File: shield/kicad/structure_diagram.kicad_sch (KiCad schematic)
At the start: 15 parts, among them J1 FCI-10118193-0001LF, J10 Amphenol SFV12R-2STE1HLF, J11 Harwin M20-8771042, J12 Harwin M20-8770842, J13 Harwin M20-8770642, J2 JST S2B-PH-SM4-TB(LF)(SN), J3 BAT_P, J4 BAT_TS, J5 BAT_M, J6 JST S3B-PH-SM4-TB(LF)(SN)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

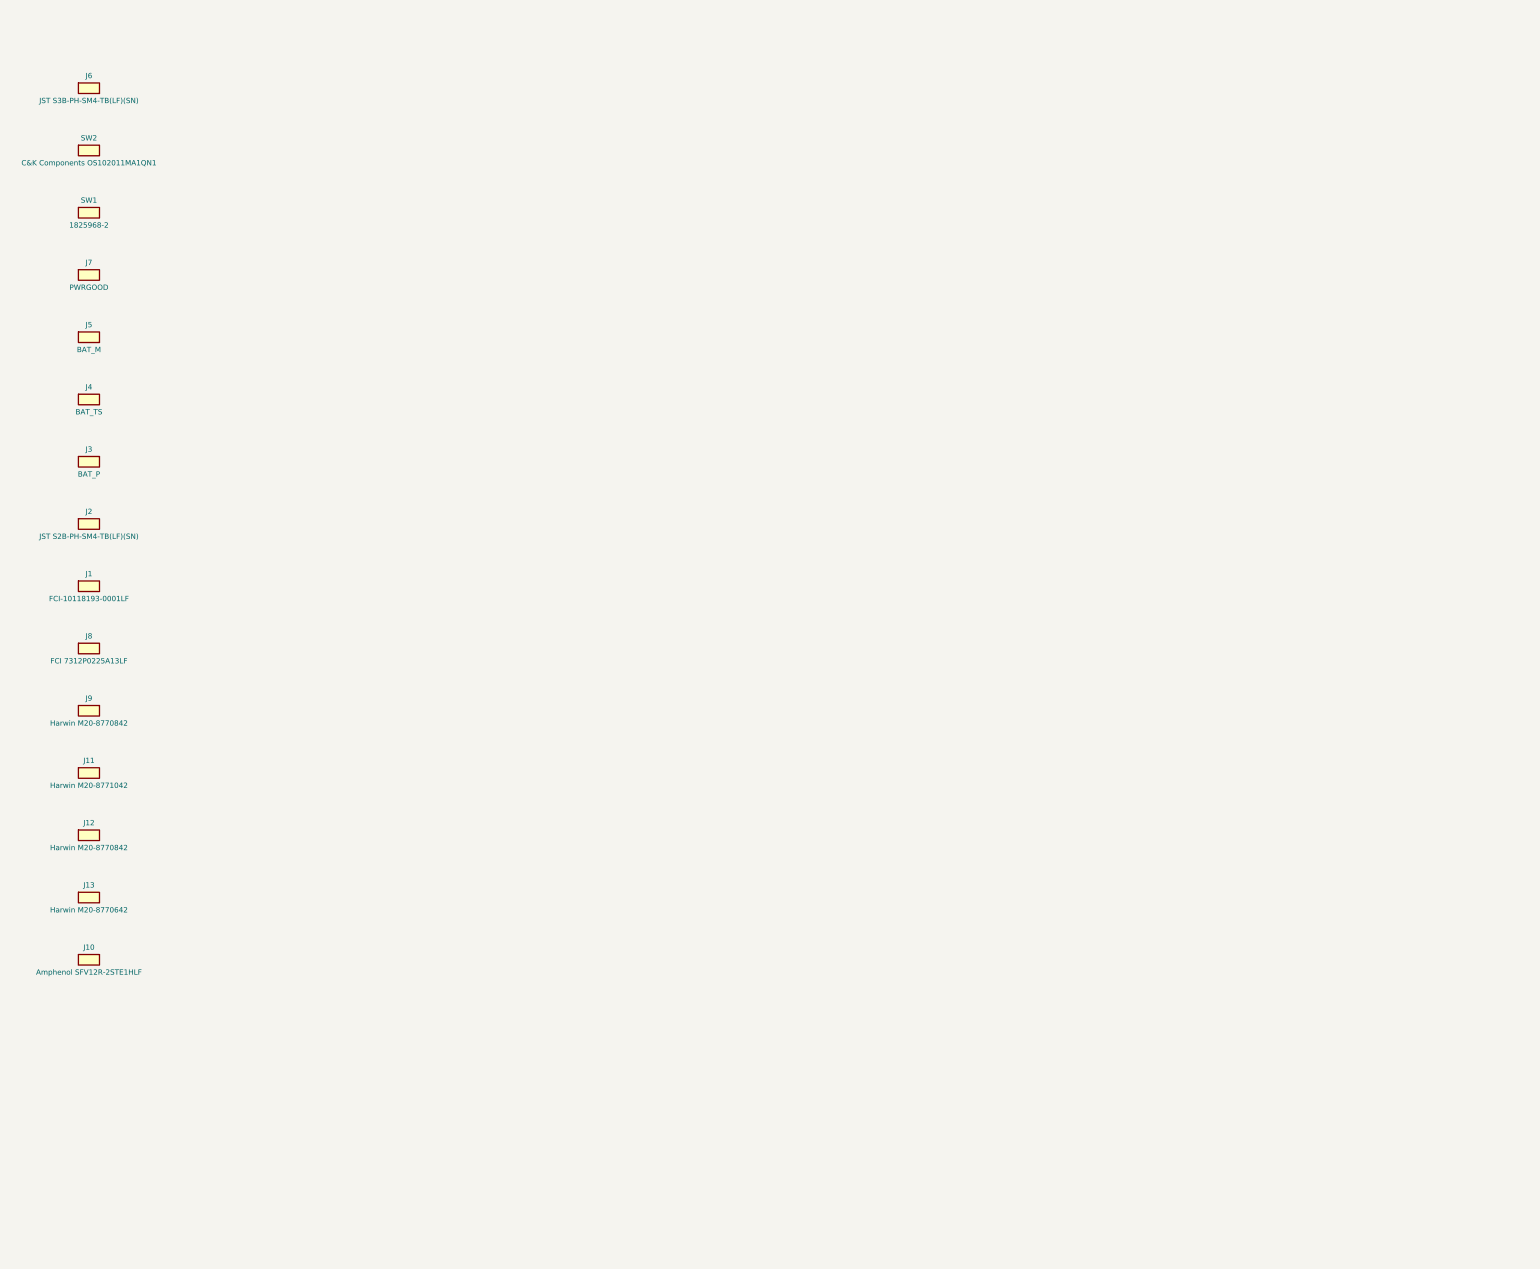
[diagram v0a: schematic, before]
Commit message: Complete schematic wiring, footprint assignments, and validation renders
- Generated proper KiCad symbols with pin definitions for all 139 components
- Created 2 hierarchical sub-sheets: Power Supply and Peripherals & Connectors
- Added schematic wiring with net labels (VBUS, VBAT, V3V3, GND, I2C, SPI, etc.)
- Assigned KiCad standard library footprints to all components
- Rendered schematic and PCB SVGs using kicad-cli-nightly
- Ran ERC and DRC validation
- Updated README with rendered images and footprint assignment table

Agent-Logs-Url: https://github.com/3rdIteration/specter-diy/sessions/67aa0d59-b533-4f87-a3fd-0109cc63ae2b

Co-authored-by: 3rdIteration <2230318+3rdIteration@users.noreply.github.com>
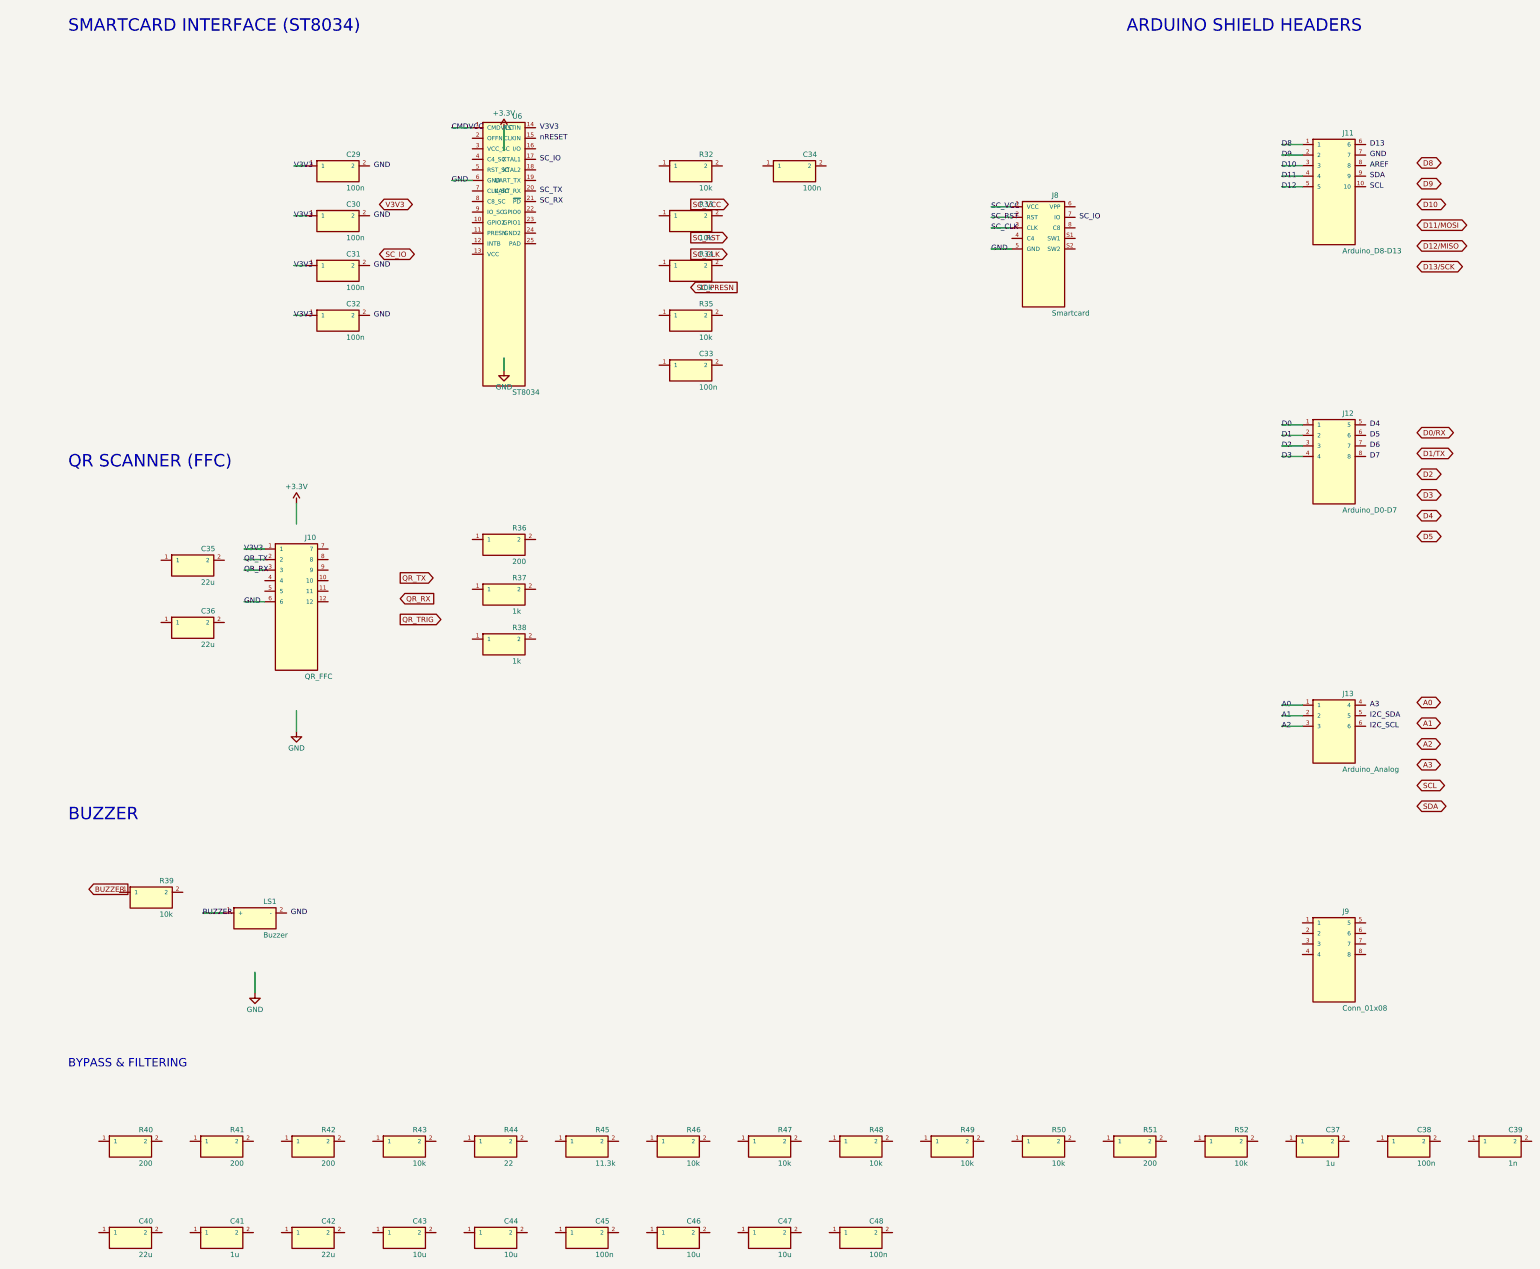
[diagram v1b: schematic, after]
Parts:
- removed J1: FCI-10118193-0001LF, MICRO-USB5+6P-SMD-0.65-B, symbol specter_shield:J1
- removed J10: Amphenol SFV12R-2STE1HLF, PCB-k5pgcgjronex5cu153ln-1, symbol specter_shield:J10
- removed J11: Harwin M20-8771042, PCB-oi3786kvfyfvus515mhx-1, symbol specter_shield:J11
- removed J12: Harwin M20-8770842, PCB-a1fsc6jjl71gcgtqmpw9-1, symbol specter_shield:J12
- removed J13: Harwin M20-8770642, PCB-tcxrerk3sfa09abtw5ob-1, symbol specter_shield:J13
- removed J2: JST S2B-PH-SM4-TB(LF)(SN), JSTPH2, symbol specter_shield:J2
- removed J3: BAT_P, PCB-zaz9lv92tniud42eyscu-1, symbol specter_shield:J3
- removed J4: BAT_TS, PCB-zaz9lv92tniud42eyscu-1, symbol specter_shield:J4
- removed J5: BAT_M, PCB-zaz9lv92tniud42eyscu-1, symbol specter_shield:J5
- removed J6: JST S3B-PH-SM4-TB(LF)(SN), PCB-icmh3e5dg0zwnj7dnv4l-1, symbol specter_shield:J6
- removed J7: PWRGOOD, PCB-16u5lfhv285szk9mzlb4-1, symbol specter_shield:J7
- removed J8: FCI 7312P0225A13LF, PCBComponent_1_-_duplicate, symbol specter_shield:J8
- removed J9: Harwin M20-8770842, PCB-a1fsc6jjl71gcgtqmpw9-1, symbol specter_shield:J9
- removed SW1: 1825968-2, PCB-y9eaa5ubtxtmw5joheuc-1, symbol specter_shield:SW1
- removed SW2: C&K Components OS102011MA1QN1, PCB-jzft20c5ocof3hhi9mdb-1, symbol specter_shield:SW2
- added C29: 100n, Capacitor_SMD:C_0402_1005Metric, symbol C29
- added C30: 100n, Capacitor_SMD:C_0402_1005Metric, symbol C30
- added C31: 100n, Capacitor_SMD:C_0402_1005Metric, symbol C31
- added C32: 100n, Capacitor_SMD:C_0402_1005Metric, symbol C32
- added C33: 100n, Capacitor_SMD:C_0402_1005Metric, symbol C33
- added C34: 100n, Capacitor_SMD:C_0402_1005Metric, symbol C34
- added C35: 22u, Capacitor_SMD:C_0805_2012Metric, symbol C35
- added C36: 22u, Capacitor_SMD:C_0805_2012Metric, symbol C36
- added C37: 1u, Capacitor_SMD:C_0402_1005Metric, symbol C37
- added C38: 100n, Capacitor_SMD:C_0402_1005Metric, symbol C38
- added C39: 1n, Capacitor_SMD:C_0402_1005Metric, symbol C39
- added C40: 22u, Capacitor_SMD:C_0805_2012Metric, symbol C40
- added C41: 1u, Capacitor_SMD:C_0402_1005Metric, symbol C41
- added C42: 22u, Capacitor_SMD:C_0805_2012Metric, symbol C42
- added C43: 10u, Capacitor_SMD:C_0805_2012Metric, symbol C43
- added C44: 10u, Capacitor_SMD:C_0805_2012Metric, symbol C44
- added C45: 100n, Capacitor_SMD:C_0402_1005Metric, symbol C45
- added C46: 10u, Capacitor_SMD:C_0805_2012Metric, symbol C46
- added C47: 10u, Capacitor_SMD:C_0805_2012Metric, symbol C47
- added C48: 100n, Capacitor_SMD:C_0402_1005Metric, symbol C48
- added J10: QR_FFC, Connector_FFC-FPC:Hirose_FH12-12S-0.5SH_1x12-1MP_P0.50mm_Horizontal, symbol J10
- added J11: Arduino_D8-D13, Connector_PinHeader_2.54mm:PinHeader_1x10_P2.54mm_Vertical, symbol J11
- added J12: Arduino_D0-D7, Connector_PinHeader_2.54mm:PinHeader_1x08_P2.54mm_Vertical, symbol J12
- added J13: Arduino_Analog, Connector_PinHeader_2.54mm:PinHeader_1x06_P2.54mm_Vertical, symbol J13
- added J8: Smartcard, Connector_Card:Smartcard_C-707-10M008-S, symbol J8
- added J9: Conn_01x08, Connector_PinHeader_2.54mm:PinHeader_1x08_P2.54mm_Vertical, symbol J9
- added LS1: Buzzer, Buzzer_Beeper:Buzzer_TDK_PS1240P02BT_D12.2mm_H6.5mm, symbol LS1
- added R32: 10k, Resistor_SMD:R_0402_1005Metric, symbol R32
- added R33: 10k, Resistor_SMD:R_0402_1005Metric, symbol R33
- added R34: 10k, Resistor_SMD:R_0402_1005Metric, symbol R34
- added R35: 10k, Resistor_SMD:R_0402_1005Metric, symbol R35
- added R36: 200, Resistor_SMD:R_0402_1005Metric, symbol R36
- added R37: 1k, Resistor_SMD:R_0402_1005Metric, symbol R37
- added R38: 1k, Resistor_SMD:R_0402_1005Metric, symbol R38
- added R39: 10k, Resistor_SMD:R_0402_1005Metric, symbol R39
- added R40: 200, Resistor_SMD:R_0402_1005Metric, symbol R40
- added R41: 200, Resistor_SMD:R_0402_1005Metric, symbol R41
- added R42: 200, Resistor_SMD:R_0402_1005Metric, symbol R42
- added R43: 10k, Resistor_SMD:R_0402_1005Metric, symbol R43
- added R44: 22, Resistor_SMD:R_0402_1005Metric, symbol R44
- added R45: 11.3k, Resistor_SMD:R_0402_1005Metric, symbol R45
- added R46: 10k, Resistor_SMD:R_0402_1005Metric, symbol R46
- added R47: 10k, Resistor_SMD:R_0402_1005Metric, symbol R47
- added R48: 10k, Resistor_SMD:R_0402_1005Metric, symbol R48
- added R49: 10k, Resistor_SMD:R_0402_1005Metric, symbol R49
- added R50: 10k, Resistor_SMD:R_0402_1005Metric, symbol R50
- added R51: 200, Resistor_SMD:R_0402_1005Metric, symbol R51
- added R52: 10k, Resistor_SMD:R_0402_1005Metric, symbol R52
- added U6: ST8034, Package_DFN_QFN:QFN-24-1EP_4x4mm_P0.5mm_EP2.45x2.45mm, symbol U6
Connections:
- new net A0: J13.1
- new net A1: J13.2
- new net A2: J13.3
- new net BUZZER: LS1.1 (+)
- new net CMDVCC: U6.1 (CMDVCC)
- new net D0: J12.1
- new net D1: J12.2
- new net D10: J11.3
- new net D11: J11.4
- new net D12: J11.5
- new net D2: J12.3
- new net D3: J12.4
- new net D8: J11.1
- new net D9: J11.2
- new net GND: J10.6, J8.5 (GND), U6.6 (GND)
- new net QR_RX: J10.3
- new net QR_TX: J10.2
- new net SC_CLK: J8.3 (CLK)
- new net SC_RST: J8.2 (RST)
- new net SC_VCC: J8.1 (VCC)
- new net V3V3: C29.1, C30.1, C31.1, C32.1, J10.1
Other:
- note added: "ARDUINO SHIELD HEADERS"
- note added: "BUZZER"
- note added: "BYPASS & FILTERING"
- note added: "QR SCANNER (FFC)"
- note added: "SMARTCARD INTERFACE (ST8034)"
- title: Specter Shield v1 - Structure Diagram -> Specter Shield v1 - Peripherals & Connectors
